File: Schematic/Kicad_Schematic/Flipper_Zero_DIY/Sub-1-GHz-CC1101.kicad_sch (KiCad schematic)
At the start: 0 parts

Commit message: finished Su-1-GHz-CC1101
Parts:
- added ANT2: Sub-1GHz Antenna A5, footprints:ANT_1001312_AVX, symbol Device:Antenna
- added C25, C26, C27, C28, C30, C36, C37: 100nF, Capacitor_SMD:C_0402_1005Metric, symbol Device:C
- added C29, C38: 100pF, Capacitor_SMD:C_0402_1005Metric, symbol Device:C
- added C31, C39, C40, C44, C89, C90, C92: DNP, Capacitor_SMD:C_0402_1005Metric, symbol Device:C
- added C32: 1.2pF, Capacitor_SMD:C_0402_1005Metric, symbol Device:C
- added C33: 0.6pF, Capacitor_SMD:C_0402_1005Metric, symbol Device:C
- added C34, C35: 9pF, Capacitor_SMD:C_0402_1005Metric, symbol Device:C
- added C42, C43: 10pF, Capacitor_SMD:C_0402_1005Metric, symbol Device:C
- added C45: 8.2pF, Capacitor_SMD:C_0402_1005Metric, symbol Device:C
- added C46, C47: 10nF, Capacitor_SMD:C_0402_1005Metric, symbol Device:C
- added C91: 22pF, Capacitor_SMD:C_0402_1005Metric, symbol Device:C
- added DD2: ~, Package_DFN_QFN:QFN-20-1EP_4x4mm_P0.5mm_EP2.5x2.5mm, symbol Flipper_Zero_Lib:CC1101RGPR
- added FLT2: ~, footprints:0805_6PIN_PACKAGE, symbol Flipper_Zero_Lib:B0310J50100AHF
- added L10: DNP, Inductor_SMD:L_0402_1005Metric, symbol Device:L
- added L11: 2.7nH, Inductor_SMD:L_0402_1005Metric, symbol Device:L
- added L16: 56nH, Inductor_SMD:L_0402_1005Metric, symbol Device:L
- added L17: 22nH, Inductor_SMD:L_0402_1005Metric, symbol Device:L
- added L18, L20, L6, L7, L8: 0, Inductor_SMD:L_0402_1005Metric, symbol Device:L
- added L19: 27nH, Inductor_SMD:L_0402_1005Metric, symbol Device:L
- added L4: 3.3nH, Inductor_SMD:L_0402_1005Metric, symbol Device:L
- added L5: 6.8nH, Inductor_SMD:L_0402_1005Metric, symbol Device:L
- added L9: 2.2nH, Inductor_SMD:L_0402_1005Metric, symbol Device:L
- added R12, R15: 0, Resistor_SMD:R_0201_0603Metric, symbol Device:R
- added R13: 56k, Resistor_SMD:R_0402_1005Metric, symbol Device:R
- added R14: 330, Resistor_SMD:R_0402_1005Metric, symbol Device:R
- added SW1, SW2: BGS13S4N9E6327XTSA1, footprints:TSNP-9-3_INF, symbol BGS13S4N9E6327XTSA1:BGS13S4N9E6327XTSA1
- added TP53: CC_PWR, TestPoint:TestPoint_Pad_1.0x1.0mm, symbol Connector:TestPoint
- added TP54: Balun, footprints:2_TEST_PIN_1.35mm_pitch, symbol Connector:TestPoint_2Pole
- added TP55: SUB-1-GHz, footprints:2_TEST_PIN_1.35mm_pitch, symbol Connector:TestPoint_2Pole
- added ZQ3: CXD2-026000000-0810B, Crystal:Crystal_SMD_2520-4Pin_2.5x2.0mm, symbol Device:Crystal_GND3
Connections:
- new net: ANT2.1 (A), C90.1, R15.2, TP55.1
- new net: C43.1, L19.2, L8.1
- new net: C40.2, L10.2, L9.1, SW2.4 (RFin)
- new net: C91.1, L17.1, L8.2
- new net: L17.2, SW2.3 (RF1)
- new net: C42.1, L19.1, L7.2
- new net: C32.1, L5.2, R12.1
- new net: R12.2, SW1.4 (RFin), TP54.1
- new net: C89.2, L16.1, L6.2
- new net: L16.2, SW2.5 (RF2)
- new net: C45.1, L11.1, L20.2
- new net: C92.1, L11.2, SW2.2 (RF3)
- new net: L7.1, SW1.5 (RF2)
- new net: C39.2, L18.2, L6.1
- new net: L20.1, SW1.2 (RF3)
- new net: L18.1, SW1.3 (RF1)
- new net: FLT2.1 (Unbal), L4.1
- new net: C29.2, FLT2.3 (Bal)
- new net: C38.2, FLT2.4 (Bal)
- new net: C35.2, DD2.10 (XOSC_Q2), ZQ3.2
- new net: C33.2, C38.1, DD2.12 (RF_P)
- new net: C29.1, C33.1, DD2.13 (RF_N)
- new net: DD2.17 (RBIAS), R13.1
- new net: C30.2, DD2.5 (DCOUPL)
- new net: DD2.6 (GDO0), R14.1
- new net: C34.2, DD2.8 (XOSC_Q1), ZQ3.1
- new net: C44.1, L9.2, R15.1
- new net: C31.1, L4.2, L5.1
- new net +3V3: C25.1, C26.1, C27.1, C28.1, C36.1, C37.1, C46.1, C47.2, DD2.11 (AVDD), DD2.14 (AVDD), DD2.15 (AVDD), DD2.18 (DGUARD), DD2.4 (DVDD), DD2.9 (AVDD), SW1.7 (VDD), SW2.7 (VDD), TP53.1
- new net CC1101_CS: DD2.7 (CSN)
- new net CC1101_G0: R14.2
- new net GNDREF: C25.2, C26.2, C27.2, C28.2, C30.1, C31.2, C32.2, C34.1, C35.1, C36.2, C37.2, C39.1, C40.1, C42.2, C43.2, C44.2, C45.2, C46.2, C47.1, C89.1, C90.2, C91.2, C92.2, DD2.16 (GND), DD2.19 (GND), DD2.21 (EPAD), FLT2.2 (GND), L10.1, R13.2, SW1.6 (DGND), SW1.9 (GND), SW2.6 (DGND), SW2.9 (GND), TP54.2, TP55.2, ZQ3.3
- new net RF_SW_0: SW1.8 (V2), SW2.1 (V1)
- new net RF_SW_1: DD2.3 (GD02), SW1.1 (V1), SW2.8 (V2)
- new net SPI_R_MISO: DD2.2 (SO)
- new net SPI_R_MOSI: DD2.20 (SI)
- new net SPI_R_SCK: DD2.1 (SCLK)
- no-connect marks 0 -> 2
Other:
- note added: "26MHz"
- company: Flipper Devices Inc. -> Originally from : Flipper Devices Inc.

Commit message: eddited some footprints
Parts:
- ANT2: footprint footprints:ANT_1001312_AVX -> footprints:Antenna_2
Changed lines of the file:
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@@
       (effects (font (size 1.27 1.27)) (justify left))
     )
-    (property "Footprint" "footprints:ANT_1001312_AVX" (at 248.285 123.19 0)
+    (property "Footprint" "footprints:Antenna_2" (at 248.285 123.19 0)
       (effects (font (size 1.27 1.27)) hide)
     )

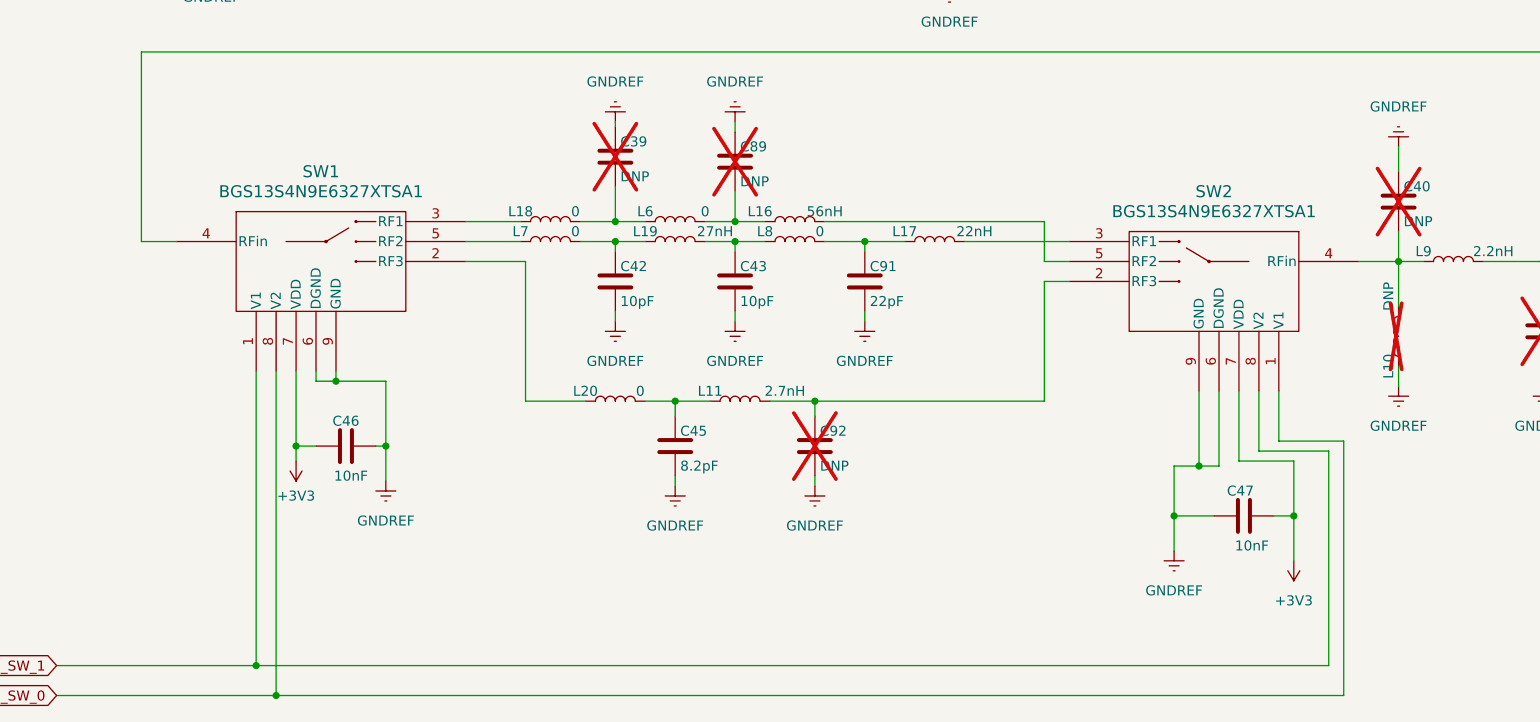
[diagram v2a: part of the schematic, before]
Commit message: replaced BGS13S4N9E6327XTSA1 (rf switch on Sub-1-GHz Schematic) with SKY13373-460LF hope it works but it looks ok
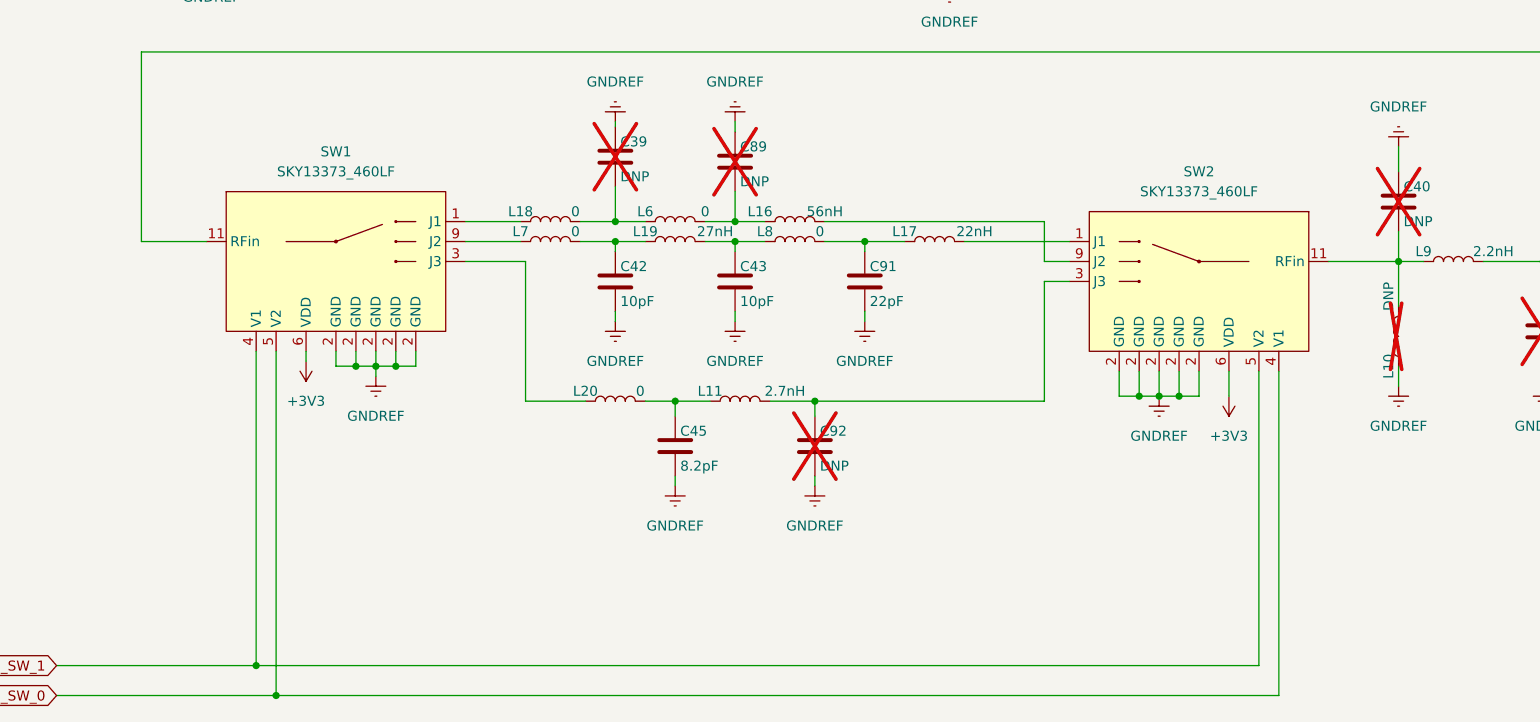
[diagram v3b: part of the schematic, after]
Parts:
- removed C46, C47: 10nF, Capacitor_SMD:C_0402_1005Metric, symbol Device:C
- removed SW1, SW2: BGS13S4N9E6327XTSA1, footprints:TSNP-9-3_INF, symbol BGS13S4N9E6327XTSA1:BGS13S4N9E6327XTSA1
- added SW1, SW2: SKY13373_460LF, symbol Flipper_Zero_Lib:SKY13373-460LF
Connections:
- net +3V3: now also SW1.6 (VDD), SW2.6 (VDD)
- net GNDREF: now also SW1.2 (GND), SW2.2 (GND)
- net RF_SW_0: now also SW1.5 (V2), SW2.4 (V1)
- net RF_SW_1: now also SW1.4 (V1), SW2.5 (V2)
- net at C40.2, L10.2, L9.1: now also SW2.11 (RFin)
- net at L17.2: now also SW2.1 (J1)
- net at R12.2, TP54.1: now also SW1.11 (RFin)
- net at L16.2: now also SW2.9 (J2)
- net at C92.1, L11.2: now also SW2.3 (J3)
- net at L7.1: now also SW1.9 (J2)
- net at L20.1: now also SW1.3 (J3)
- net at L18.1: now also SW1.1 (J1)

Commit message: added all changes to the changelog
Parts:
- added C46-1, C46-2: 100pF, symbol Device:C
- FLT2: value ~ -> B0310J50100AHF
- SW1: value SKY13373_460LF -> SKY13373-460LF; footprint (none) -> footprints:QFN-12-2x2mm_equal_distribution
- SW2: value SKY13373_460LF -> ~; footprint (none) -> footprints:QFN-12-2x2mm_equal_distribution
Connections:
- net GNDREF: now also SW1.10 (GND), SW1.12 (GND), SW1.7 (GND), SW1.8 (GND), SW2.10 (GND), SW2.12 (GND), SW2.7 (GND), SW2.8 (GND), C46-1.2, C46-2.2
- net RF_SW_0: now also C46-2.1
- net RF_SW_1: now also C46-1.1
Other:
- note added: "Added C46-1 and C46-2 for SKY13373-460LF (see documentation)"
- note added: "Freq. Selection"
- note added: "Maybe doesn't work! (3V3 is max control voltage)"
- note added: "Sub 1 GHz Transceiver"

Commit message: finished iBtn PCB
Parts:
- C46-1, C46-2: footprint (none) -> Capacitor_SMD:C_0402_1005Metric
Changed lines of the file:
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@@
       (effects (font (size 1.27 1.27)) (justify left))
     )
-    (property "Footprint" "" (at 56.8452 193.675 0)
+    (property "Footprint" "Capacitor_SMD:C_0402_1005Metric" (at 56.8452 193.675 0)
       (effects (font (size 1.27 1.27)) hide)
     )
@@
       (effects (font (size 1.27 1.27)) (justify left))
     )
-    (property "Footprint" "" (at 46.0502 193.675 0)
-      (effects (font (size 1.27 1.27)) hide)
-    )
+    (property "Footprint" "Capacitor_SMD:C_0402_1005Metric" (at 46.0502 193.675 0)
+      (effects (font (size 1.27 1.27)) hide)
+    )
